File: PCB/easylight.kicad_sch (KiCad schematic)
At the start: 51 parts, among them J1 LiPo (1S/3.7V), J2 USB/PWR, J3 LEDs, J4 AVR-ISP, J5 SW1, J6 SW1, J7 SW1, Q1 AO3415_C181094, Q2 AO3415_C181094, SW0 SPEF110100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

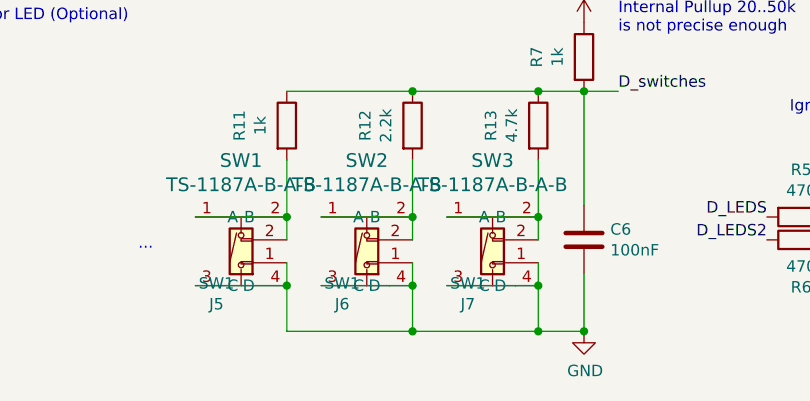
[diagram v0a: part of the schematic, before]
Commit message: relink schematics and footprints, move C, update everything
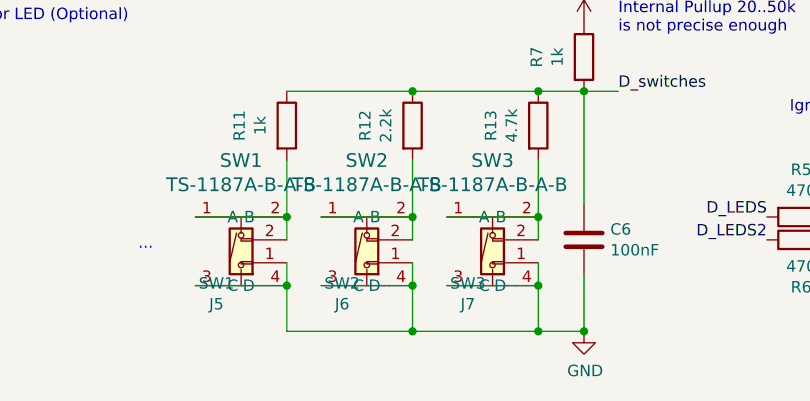
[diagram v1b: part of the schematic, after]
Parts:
- D1: footprint lcsc:SMB_L4.6-W3.6-LS5.3-BI -> LCSC:SMB_L4.6-W3.6-LS5.3-BI
- D3: footprint lcsc:SMA_L4.3-W2.6-LS5.2-RD -> LCSC:SMA_L4.3-W2.6-LS5.2-RD
- J6: value SW1 -> SW2
- J7: value SW1 -> SW3
- R1, R10, R11, R12, R13, R2, R3, R4, R5, R6, R7, R9: footprint Resistor_SMD:R_0603_1608Metric_Pad1.05x0.95mm_HandSolder -> Resistor_SMD:R_0603_1608Metric_Pad0.98x0.95mm_HandSolder
- SW0: footprint lcsc:SW-TH_SPEF110100_fixed -> LCSC:SW-TH_SPEF110100_fixed
- SW1, SW2, SW3: footprint lcsc:SW-SMD_4P-L5.1-W5.1-P3.70-LS6.5-TL-2 -> LCSC:SW-SMD_4P-L5.1-W5.1-P3.70-LS6.5-TL-2
- U2: footprint lcsc:SOT-23-6_L2.9-W1.6-P0.95-LS2.8-BR -> LCSC:SOT-23-6_L2.9-W1.6-P0.95-LS2.8-BR
- U3: footprint lcsc:SOIC-8_L4.9-W3.9-P1.27-LS6.0-BL-EP3.3-1 -> LCSC:SOIC-8_L4.9-W3.9-P1.27-LS6.0-BL-EP3.3-1

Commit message: update readme, cleanup libs
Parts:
- D1: symbol easylight-rescue:P6SMB6.8CA-C78395-LCSC -> LCSC:P6SMB6.8CA-C78395-LCSC
- D3: symbol easylight-rescue:SS34_C8678-LCSC -> LCSC:SS34_C8678-LCSC
- G1: symbol easylight-rescue:LOGO-WEEEE -> ModischFabrications:LOGO-WEEEE
- L1, L2: symbol easylight-rescue:LOGO-MPC -> ModischFabrications:LOGO-MPC
- Q1, Q2: symbol easylight-rescue:AO3415_C181094-LCSC -> LCSC:AO3415_C181094-LCSC
- SW0: symbol easylight-rescue:SPEF110100-LCSC -> LCSC:SPEF110100-LCSC
- SW1, SW2, SW3: symbol easylight-rescue:TS-1187A-B-A-B-LCSC -> LCSC:TS-1187A-B-A-B-LCSC
- U1: symbol easylight-rescue:ATtiny85-20PU-MCU_Microchip_ATtiny -> MCU_Microchip_ATtiny:ATtiny85-20P
- U2: symbol easylight-rescue:BQ21040DBVR-LCSC -> LCSC:BQ21040DBVR-LCSC
- U3: symbol easylight-rescue:XB8089D0-LCSC -> LCSC:XB8089D0-LCSC
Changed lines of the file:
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@@
     (pin "1")
   )
-  (symbol (lib_id "easylight-rescue:ATtiny85-20PU-MCU_Microchip_ATtiny") (at 44.45 121.92 0) (unit 1)
+  (symbol (lib_id "MCU_Microchip_ATtiny:ATtiny85-20P") (at 44.45 121.92 0) (unit 1)
     (in_bom yes) (on_board yes)
     (property "Reference" "U1" (id 0) (at 31.0134 120.7516 0)
@@
     (pin "2")
   )
-  (symbol (lib_id "easylight-rescue:XB8089D0-LCSC") (at 259.08 113.03 180) (unit 1)
+  (symbol (lib_id "LCSC:XB8089D0-LCSC") (at 259.08 113.03 180) (unit 1)
     (in_bom yes) (on_board yes)
     (property "Reference" "U3" (id 0) (at 259.08 100.6602 0)
@@
     (pin "2")
   )
-  (symbol (lib_id "easylight-rescue:BQ21040DBVR-LCSC") (at 120.65 33.02 0) (mirror y) (unit 1)
+  (symbol (lib_id "LCSC:BQ21040DBVR-LCSC") (at 120.65 33.02 0) (mirror y) (unit 1)
     (in_bom yes) (on_board yes)
     (property "Reference" "U2" (id 0) (at 120.65 23.1902 0)
@@
     (pin "6")
   )
-  (symbol (lib_id "easylight-rescue:AO3415_C181094-LCSC") (at 222.25 45.72 0) (unit 1)
+  (symbol (lib_id "LCSC:AO3415_C181094-LCSC") (at 222.25 45.72 0) (unit 1)
     (in_bom yes) (on_board yes)
     (property "Reference" "Q1" (id 0) (at 230.0732 44.3738 0)
@@
     (pin "2")
   )
-  (symbol (lib_id "easylight-rescue:SS34_C8678-LCSC") (at 214.63 58.42 180) (unit 1)
+  (symbol (lib_id "LCSC:SS34_C8678-LCSC") (at 214.63 58.42 180) (unit 1)
     (in_bom yes) (on_board yes)
     (property "Reference" "D3" (id 0) (at 214.63 51.6382 0)
@@
     (pin "2")
   )
-  (symbol (lib_id "easylight-rescue:AO3415_C181094-LCSC") (at 53.34 35.56 90) (unit 1)
+  (symbol (lib_id "LCSC:AO3415_C181094-LCSC") (at 53.34 35.56 90) (unit 1)
     (in_bom yes) (on_board yes)
     (property "Reference" "Q2" (id 0) (at 51.9938 27.7368 0)
@@
     (pin "2")
   )
-  (symbol (lib_id "easylight-rescue:P6SMB6.8CA-C78395-LCSC") (at 41.91 43.18 270) (unit 1)
+  (symbol (lib_id "LCSC:P6SMB6.8CA-C78395-LCSC") (at 41.91 43.18 270) (unit 1)
     (in_bom yes) (on_board yes)
     (property "Reference" "D1" (id 0) (at 44.1452 41.8338 90)
@@
     (pin "1")
   )
-  (symbol (lib_name "TS-1187A-B-A-B-LCSC_1") (lib_id "easylight-rescue:TS-1187A-B-A-B-LCSC") (at 93.98 179.07 0) (unit 1)
+  (symbol (lib_id "LCSC:TS-1187A-B-A-B-LCSC") (at 93.98 179.07 0) (unit 1)
     (in_bom yes) (on_board yes)
     (property "Reference" "SW3" (id 0) (at 93.98 170.2562 0)
@@
     (pin "4")
   )
-  (symbol (lib_name "TS-1187A-B-A-B-LCSC_2") (lib_id "easylight-rescue:TS-1187A-B-A-B-LCSC") (at 80.01 179.07 0) (unit 1)
+  (symbol (lib_id "LCSC:TS-1187A-B-A-B-LCSC") (at 80.01 179.07 0) (unit 1)
     (in_bom yes) (on_board yes)
     (property "Reference" "SW2" (id 0) (at 80.01 170.2562 0)
@@
     (pin "4")
   )
-  (symbol (lib_id "easylight-rescue:TS-1187A-B-A-B-LCSC") (at 66.04 179.07 0) (unit 1)
+  (symbol (lib_id "LCSC:TS-1187A-B-A-B-LCSC") (at 66.04 179.07 0) (unit 1)
     (in_bom yes) (on_board yes)
     (property "Reference" "SW1" (id 0) (at 66.04 170.2562 0)
@@
     (pin "1")
   )
-  (symbol (lib_id "easylight-rescue:SPEF110100-LCSC") (at 246.38 57.15 0) (unit 1)
+  (symbol (lib_id "LCSC:SPEF110100-LCSC") (at 246.38 57.15 0) (unit 1)
     (in_bom yes) (on_board yes)
     (property "Reference" "SW0" (id 0) (at 246.38 49.6062 0)
@@
     (pin "1")
   )
-  (symbol (lib_id "easylight-rescue:LOGO-MPC") (at 193.04 173.99 0) (unit 1)
+  (symbol (lib_id "ModischFabrications:LOGO-MPC") (at 193.04 173.99 0) (unit 1)
     (in_bom yes) (on_board yes)
     (property "Reference" "L1" (id 0) (at 193.04 176.1744 0)
@@
     (pin "1")
   )
-  (symbol (lib_id "easylight-rescue:LOGO-WEEEE") (at 266.7 173.99 0) (unit 1)
+  (symbol (lib_id "ModischFabrications:LOGO-WEEEE") (at 266.7 173.99 0) (unit 1)
     (in_bom yes) (on_board yes)
     (property "Reference" "G1" (id 0) (at 266.7 180.6702 0)
@@
     (pin "2")
   )
-  (symbol (lib_id "easylight-rescue:LOGO-MPC") (at 171.45 88.9 0) (unit 1)
+  (symbol (lib_id "ModischFabrications:LOGO-MPC") (at 171.45 88.9 0) (unit 1)
     (in_bom yes) (on_board yes)
     (property "Reference" "L2" (id 0) (at 171.45 91.0844 0)

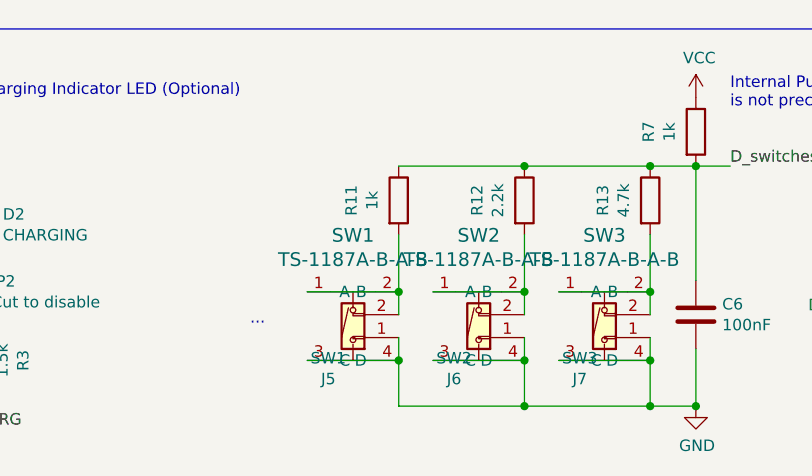
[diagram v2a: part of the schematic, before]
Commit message: remove colliding connector, add button extension connector, declare v1.0
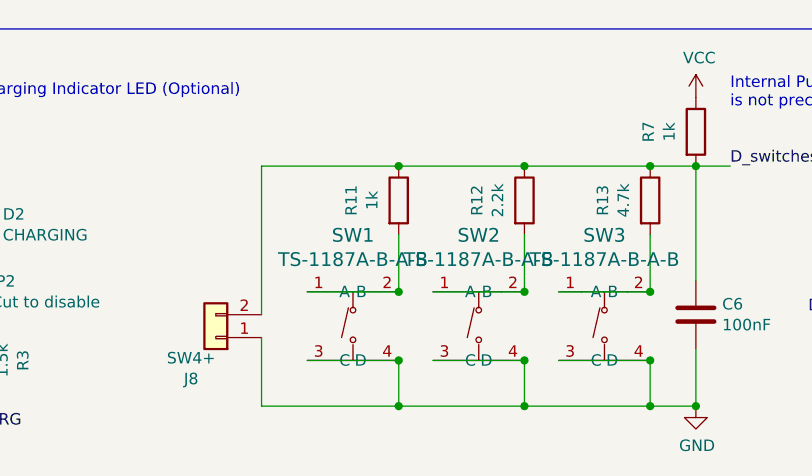
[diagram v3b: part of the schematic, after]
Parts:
- removed J5: SW1, Connector_PinHeader_2.54mm:PinHeader_1x02_P2.54mm_Vertical, symbol Connector_Generic:Conn_01x02
- removed J6: SW2, Connector_PinHeader_2.54mm:PinHeader_1x02_P2.54mm_Vertical, symbol Connector_Generic:Conn_01x02
- removed J7: SW3, Connector_PinHeader_2.54mm:PinHeader_1x02_P2.54mm_Vertical, symbol Connector_Generic:Conn_01x02
- added J8: SW4+, Connector_PinHeader_2.54mm:PinHeader_1x02_P2.54mm_Vertical, symbol Connector_Generic:Conn_01x02
- J1, J2: LCSC Part (none) -> C158012
- J3: LCSC Part (none) -> C144395
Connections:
- net D_switches: now also J8.2 (Pin_2)
- net GND: now also J8.1 (Pin_1)
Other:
- note removed: "..."
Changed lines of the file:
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@@
   (title_block
     (title "EasyLight")
-    (date "2023-01-24")
-    (rev "1")
+    (date "2023-01-29")
+    (rev "1.0")
     (company "MPC")
   )
@@
   (junction (at 213.36 118.11) (diameter 0) (color 0 0 0 0)
   )
+  (junction (at 71.12 162.56) (diameter 0) (color 0 0 0 0)
+  )
   (junction (at 232.41 118.11) (diameter 0) (color 0 0 0 0)
   )
@@
   )
   (junction (at 99.06 176.53) (diameter 0) (color 0 0 0 0)
+  )
+  (junction (at 71.12 189.23) (diameter 0) (color 0 0 0 0)
   )
   (junction (at 71.12 184.15) (diameter 0) (color 0 0 0 0)
@@
     (stroke (width 0) (type default) (color 0 0 0 0))
   )
+  (wire (pts (xy 55.88 162.56) (xy 71.12 162.56))
+    (stroke (width 0) (type default) (color 0 0 0 0))
+  )
   (wire (pts (xy 227.33 35.56) (xy 227.33 40.64))
     (stroke (width 0) (type default) (color 0 0 0 0))
@@
     (stroke (width 0) (type default) (color 0 0 0 0))
   )
-  (wire (pts (xy 85.09 181.61) (xy 85.09 184.15))
-    (stroke (width 0) (type default) (color 0 0 0 0))
-  )
   (wire (pts (xy 87.63 45.72) (xy 87.63 50.8))
     (stroke (width 0) (type default) (color 0 0 0 0))
@@
     (stroke (width 0) (type default) (color 0 0 0 0))
   )
-  (wire (pts (xy 71.12 179.07) (xy 71.12 176.53))
-    (stroke (width 0) (type default) (color 0 0 0 0))
-  )
   (wire (pts (xy 227.33 110.49) (xy 232.41 110.49))
     (stroke (width 0) (type default) (color 0 0 0 0))
   )
-  (wire (pts (xy 99.06 179.07) (xy 99.06 176.53))
-    (stroke (width 0) (type default) (color 0 0 0 0))
-  )
   (wire (pts (xy 85.09 184.15) (xy 85.09 189.23))
     (stroke (width 0) (type default) (color 0 0 0 0))
   )
+  (wire (pts (xy 55.88 189.23) (xy 55.88 181.61))
+    (stroke (width 0) (type default) (color 0 0 0 0))
+  )
   (wire (pts (xy 41.91 50.8) (xy 41.91 48.26))
     (stroke (width 0) (type default) (color 0 0 0 0))
@@
     (stroke (width 0) (type default) (color 0 0 0 0))
   )
+  (wire (pts (xy 55.88 179.07) (xy 55.88 162.56))
+    (stroke (width 0) (type default) (color 0 0 0 0))
+  )
   (polyline (pts (xy 80.01 16.51) (xy 80.01 64.77))
     (stroke (width 0) (type default) (color 0 0 0 0))
@@
     (stroke (width 0) (type default) (color 0 0 0 0))
   )
-  (wire (pts (xy 99.06 181.61) (xy 99.06 184.15))
-    (stroke (width 0) (type default) (color 0 0 0 0))
-  )
   (wire (pts (xy 104.14 182.88) (xy 104.14 189.23))
     (stroke (width 0) (type default) (color 0 0 0 0))
@@
     (stroke (width 0) (type default) (color 0 0 0 0))
   )
-  (wire (pts (xy 85.09 179.07) (xy 85.09 176.53))
-    (stroke (width 0) (type default) (color 0 0 0 0))
-  )
   (wire (pts (xy 99.06 184.15) (xy 99.06 189.23))
     (stroke (width 0) (type default) (color 0 0 0 0))
@@
     (stroke (width 0) (type default) (color 0 0 0 0))
   )
-  (wire (pts (xy 71.12 181.61) (xy 71.12 184.15))
+  (wire (pts (xy 71.12 189.23) (xy 55.88 189.23))
     (stroke (width 0) (type default) (color 0 0 0 0))
   )
@@
   )
   (text "Low while charging\nUse LED or PB4" (at 120.65 43.18 0)
-    (effects (font (size 1.27 1.27)) (justify left bottom))
-  )
-  (text "..." (at 54.61 180.34 0)
     (effects (font (size 1.27 1.27)) (justify left bottom))
   )
@@
     )
     (property "Datasheet" "~" (id 3) (at 24.13 39.37 0)
+      (effects (font (size 1.27 1.27)) hide)
+    )
+    (property "LCSC Part" "C158012" (id 4) (at 24.13 39.37 0)
       (effects (font (size 1.27 1.27)) hide)
     )
@@
     )
     (property "Datasheet" "~" (id 3) (at 208.28 118.11 0)
+      (effects (font (size 1.27 1.27)) hide)
+    )
+    (property "LCSC Part" "C158012" (id 4) (at 208.28 118.11 0)
       (effects (font (size 1.27 1.27)) hide)
     )
@@
     (pin "2")
   )
-  (symbol (lib_id "Connector_Generic:Conn_01x02") (at 66.04 181.61 180) (unit 1)
-    (in_bom yes) (on_board yes)
-    (property "Reference" "J5" (id 0) (at 63.2968 186.2074 0))
-    (property "Value" "SW1" (id 1) (at 63.2968 183.896 0))
-    (property "Footprint" "Connector_PinHeader_2.54mm:PinHeader_1x02_P2.54mm_Vertical" (id 2) (at 66.04 181.61 0)
-      (effects (font (size 1.27 1.27)) hide)
-    )
-    (property "Datasheet" "~" (id 3) (at 66.04 181.61 0)
-      (effects (font (size 1.27 1.27)) hide)
-    )
-    (pin "1")
-    (pin "2")
-  )
   (symbol (lib_id "Connector_Generic:Conn_01x04") (at 140.97 176.53 0) (unit 1)
     (in_bom yes) (on_board yes)
@@
     )
     (property "Datasheet" "~" (id 3) (at 140.97 176.53 0)
+      (effects (font (size 1.27 1.27)) hide)
+    )
+    (property "LCSC Part" "C144395" (id 4) (at 140.97 176.53 0)
       (effects (font (size 1.27 1.27)) hide)
     )
@@
     )
     (pin "1")
-  )
-  (symbol (lib_id "Connector_Generic:Conn_01x02") (at 80.01 181.61 180) (unit 1)
-    (in_bom yes) (on_board yes)
-    (property "Reference" "J6" (id 0) (at 77.2668 186.2074 0))
-    (property "Value" "SW2" (id 1) (at 77.2668 183.896 0))
-    (property "Footprint" "Connector_PinHeader_2.54mm:PinHeader_1x02_P2.54mm_Vertical" (id 2) (at 80.01 181.61 0)
-      (effects (font (size 1.27 1.27)) hide)
-    )
-    (property "Datasheet" "~" (id 3) (at 80.01 181.61 0)
-      (effects (font (size 1.27 1.27)) hide)
-    )
-    (pin "1")
-    (pin "2")
-  )
-  (symbol (lib_id "Connector_Generic:Conn_01x02") (at 93.98 181.61 180) (unit 1)
-    (in_bom yes) (on_board yes)
-    (property "Reference" "J7" (id 0) (at 91.2368 186.2074 0))
-    (property "Value" "SW3" (id 1) (at 91.2368 183.896 0))
-    (property "Footprint" "Connector_PinHeader_2.54mm:PinHeader_1x02_P2.54mm_Vertical" (id 2) (at 93.98 181.61 0)
-      (effects (font (size 1.27 1.27)) hide)
-    )
-    (property "Datasheet" "~" (id 3) (at 93.98 181.61 0)
-      (effects (font (size 1.27 1.27)) hide)
-    )
-    (pin "1")
-    (pin "2")
   )
   (symbol (lib_id "Connector:AVR-ISP-6") (at 151.13 124.46 0) (unit 1)
@@
     (pin "2")
   )
+  (symbol (lib_id "Connector_Generic:Conn_01x02") (at 50.8 181.61 180) (unit 1)
+    (in_bom yes) (on_board yes)
+    (property "Reference" "J8" (id 0) (at 48.0568 186.2074 0))
+    (property "Value" "SW4+" (id 1) (at 48.0568 183.896 0))
+    (property "Footprint" "Connector_PinHeader_2.54mm:PinHeader_1x02_P2.54mm_Vertical" (id 2) (at 50.8 181.61 0)
+      (effects (font (size 1.27 1.27)) hide)
+    )
+    (property "Datasheet" "~" (id 3) (at 50.8 181.61 0)
+      (effects (font (size 1.27 1.27)) hide)
+    )
+    (pin "1")
+    (pin "2")
+  )
   (symbol (lib_id "ModischFabrications:LOGO-MPC") (at 171.45 88.9 0) (unit 1)
     (in_bom yes) (on_board yes)
@@
       (reference "J4") (unit 1) (value "AVR-ISP") (footprint "Connector_PinHeader_2.54mm:PinHeader_2x03_P2.54mm_Vertical")
     )
-    (path "/00000000-0000-0000-0000-000063f1188a"
-      (reference "J5") (unit 1) (value "SW1") (footprint "Connector_PinHeader_2.54mm:PinHeader_1x02_P2.54mm_Vertical")
-    )
-    (path "/00000000-0000-0000-0000-000063f17d06"
-      (reference "J6") (unit 1) (value "SW2") (footprint "Connector_PinHeader_2.54mm:PinHeader_1x02_P2.54mm_Vertical")
-    )
-    (path "/00000000-0000-0000-0000-000063f183c0"
-      (reference "J7") (unit 1) (value "SW3") (footprint "Connector_PinHeader_2.54mm:PinHeader_1x02_P2.54mm_Vertical")
+    (path "/7077f794-b698-44e0-8cf7-3d3000ab4c20"
+      (reference "J8") (unit 1) (value "SW4+") (footprint "Connector_PinHeader_2.54mm:PinHeader_1x02_P2.54mm_Vertical")
     )
     (path "/00000000-0000-0000-0000-000063c53736"

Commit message: use specific isp connector that has polarity marker, update revision to v1.1, set board colors
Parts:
- J4: footprint Connector_PinHeader_2.54mm:PinHeader_2x03_P2.54mm_Vertical -> ModischFabrications:3x2 CopperPad 2.54mm
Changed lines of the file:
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@@
   (title_block
     (title "EasyLight")
-    (date "2023-01-29")
-    (rev "1.0")
+    (date "2023-02-03")
+    (rev "1.1")
     (company "MPC")
   )
@@
       (effects (font (size 1.27 1.27)) (justify right))
     )
-    (property "Footprint" "Connector_PinHeader_2.54mm:PinHeader_2x03_P2.54mm_Vertical" (id 2) (at 144.78 123.19 90)
+    (property "Footprint" "ModischFabrications:3x2 CopperPad 2.54mm" (id 2) (at 144.78 123.19 90)
       (effects (font (size 1.27 1.27)) hide)
     )
@@
     )
     (path "/00000000-0000-0000-0000-000063f240fe"
-      (reference "J4") (unit 1) (value "AVR-ISP") (footprint "Connector_PinHeader_2.54mm:PinHeader_2x03_P2.54mm_Vertical")
+      (reference "J4") (unit 1) (value "AVR-ISP") (footprint "ModischFabrications:3x2 CopperPad 2.54mm")
     )
     (path "/7077f794-b698-44e0-8cf7-3d3000ab4c20"

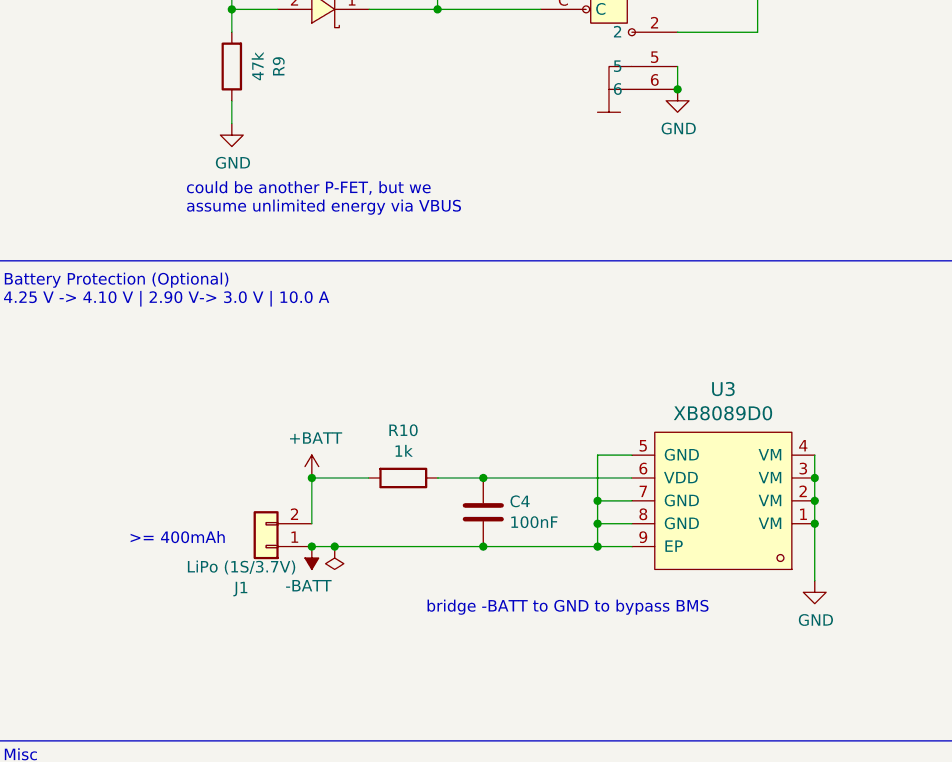
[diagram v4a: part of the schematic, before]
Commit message: add more labels, replace broken SOT23 with generic part, update version, cleanup part descriptions
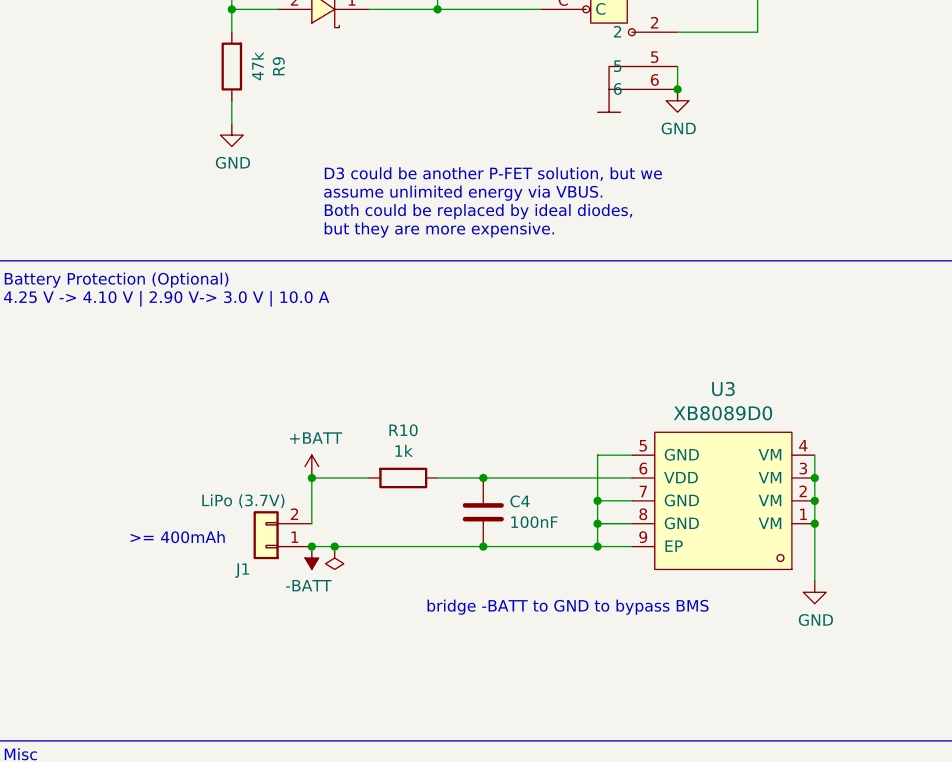
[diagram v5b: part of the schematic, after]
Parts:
- C8: footprint Capacitor_SMD:C_1206_3216Metric_Pad1.42x1.75mm_HandSolder -> Capacitor_SMD:C_1206_3216Metric_Pad1.33x1.80mm_HandSolder
- F1, J2, J3, U1: JLC Part (none) -> Extended Part
- J1: value LiPo (1S/3.7V) -> LiPo (3.7V); JLC Part (none) -> Extended Part
- Q1, Q2: footprint lcsc:SOT-23-3_L2.9-W1.3-P1.90-LS2.4-BR -> Package_TO_SOT_SMD:SOT-23-3
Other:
- note added: "D3 could be another P-FET solution, but we assume unlimited energy via VBUS. Both could be replaced by ideal diodes, but they are more expensive."
- note removed: "could be another P-FET, but we assume unlimited energy via VBUS"

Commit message: use generic part for SOIC-8, ignore another lib warning
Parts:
- U3: footprint LCSC:SOIC-8_L4.9-W3.9-P1.27-LS6.0-BL-EP3.3-1 -> Package_SO:SOIC-8-1EP_3.9x4.9mm_P1.27mm_EP2.514x3.2mm
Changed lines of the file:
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@@
       (effects (font (size 1.524 1.524)))
     )
-    (property "Footprint" "LCSC:SOIC-8_L4.9-W3.9-P1.27-LS6.0-BL-EP3.3-1" (id 2) (at 259.08 100.33 0)
+    (property "Footprint" "Package_SO:SOIC-8-1EP_3.9x4.9mm_P1.27mm_EP2.514x3.2mm" (id 2) (at 259.08 100.33 0)
       (effects (font (size 1.524 1.524)) hide)
     )
@@
     )
     (path "/00000000-0000-0000-0000-000063be38c8"
-      (reference "U3") (unit 1) (value "XB8089D0") (footprint "LCSC:SOIC-8_L4.9-W3.9-P1.27-LS6.0-BL-EP3.3-1")
-    )
-  )
+      (reference "U3") (unit 1) (value "XB8089D0") (footprint "Package_SO:SOIC-8-1EP_3.9x4.9mm_P1.27mm_EP2.514x3.2mm")
+    )
+  )
